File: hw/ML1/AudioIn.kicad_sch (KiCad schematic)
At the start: 23 parts, among them T2 Transformer_1P_1S, U1 LMV324 (Actually LTV9161), U5 LTV-356T

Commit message: Re-work of ML1 board in process
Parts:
- C19, C20: footprint KiCad-Library:CAP_KEMET_530_530 -> bruce-footprints:CAP_KEMET_530_530
- RV2: footprint KiCad-Library:POT_3362P -> bruce-footprints:POT_3362P
- T2: footprint KiCad-Library:CheapAudioTransformer -> bruce-footprints:CheapAudioTransformer
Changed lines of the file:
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@@
       (effects (font (size 1.27 1.27)))
     )
-    (property "Footprint" "KiCad-Library:CheapAudioTransformer" (at 49.53 63.5 0)
+    (property "Footprint" "bruce-footprints:CheapAudioTransformer" (at 49.53 63.5 0)
       (effects (font (size 1.27 1.27)) hide)
     )
@@
       (effects (font (size 1.27 1.27)) (justify right))
     )
-    (property "Footprint" "KiCad-Library:POT_3362P" (at 74.93 62.23 0)
+    (property "Footprint" "bruce-footprints:POT_3362P" (at 74.93 62.23 0)
       (effects (font (size 1.27 1.27)) hide)
     )
@@
       (effects (font (size 1.27 1.27)) (justify left))
     )
-    (property "Footprint" "KiCad-Library:CAP_KEMET_530_530" (at 110.49 88.9 0)
+    (property "Footprint" "bruce-footprints:CAP_KEMET_530_530" (at 110.49 88.9 0)
       (effects (font (size 1.27 1.27)) hide)
     )
@@
       (effects (font (size 1.27 1.27)) (justify left))
     )
-    (property "Footprint" "KiCad-Library:CAP_KEMET_530_530" (at 227.33 34.29 0)
-      (effects (font (size 1.27 1.27)) hide)
-    )
+    (property "Footprint" "bruce-footprints:CAP_KEMET_530_530" (at 227.33 34.29 0)
+      (effects (font (size 1.27 1.27)) hide)
+    )

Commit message: Re-work of ML1 board in process
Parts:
- removed C19: 47u, bruce-footprints:CAP_KEMET_530_530, symbol Device:C_Polarized_US
- removed C20: 100u, bruce-footprints:CAP_KEMET_530_530, symbol Device:C_Polarized_US
- added C19, C20: 47u, Capacitor_SMD:C_0805_2012Metric_Pad1.18x1.45mm_HandSolder, symbol Device:C
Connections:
- net +3.3VA: now also C20.1
- net GNDA: now also C19.2, C20.2
- net at R12.1: now also C19.1
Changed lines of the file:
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@@
+    )
+  )
+  (symbol (lib_id "Device:C") (at 227.33 34.29 0) (unit 1)
+    (in_bom yes) (on_board yes) (dnp no) (fields_autoplaced)
+    (property "Reference" "C20" (at 231.14 33.02 0)
+      (effects (font (size 1.27 1.27)) (justify left))
+    )
+    (property "Value" "47u" (at 231.14 35.56 0)
+      (effects (font (size 1.27 1.27)) (justify left))
+    )
+    (property "Footprint" "Capacitor_SMD:C_0805_2012Metric_Pad1.18x1.45mm_HandSolder" (at 228.2952 38.1 0)
+      (effects (font (size 1.27 1.27)) hide)
+    )
+    (property "Datasheet" "~" (at 227.33 34.29 0)
+      (effects (font (size 1.27 1.27)) hide)
+    )
+    (pin "1")
+    (pin "2")
+    (instances
+      (project "ML1"
+        (path "/5f8f636b-fd0e-498e-8696-0a023acb4c09/605cddf5-737f-47be-b5fd-7ed3decef4e0"
+          (reference "C20") (unit 1)
+        )
+      )
     )
   )
@@
     )
   )
-  (symbol (lib_id "Device:C_Polarized_US") (at 110.49 88.9 0) (unit 1)
-    (in_bom yes) (on_board yes) (dnp no) (fields_autoplaced)
-    (property "Reference" "C19" (at 114.3 86.995 0)
-      (effects (font (size 1.27 1.27)) (justify left))
-    )
-    (property "Value" "47u" (at 114.3 89.535 0)
-      (effects (font (size 1.27 1.27)) (justify left))
-    )
-    (property "Footprint" "bruce-footprints:CAP_KEMET_530_530" (at 110.49 88.9 0)
+  (symbol (lib_id "Device:R_US") (at 127 48.26 90) (unit 1)
+    (in_bom yes) (on_board yes) (dnp no) (fields_autoplaced)
+    (property "Reference" "R13" (at 127 41.91 90)
+      (effects (font (size 1.27 1.27)))
+    )
+    (property "Value" "2.2k" (at 127 44.45 90)
+      (effects (font (size 1.27 1.27)))
+    )
+    (property "Footprint" "Resistor_SMD:R_0805_2012Metric_Pad1.20x1.40mm_HandSolder" (at 127.254 47.244 90)
+      (effects (font (size 1.27 1.27)) hide)
+    )
+    (property "Datasheet" "~" (at 127 48.26 0)
+      (effects (font (size 1.27 1.27)) hide)
+    )
+    (pin "2")
+    (pin "1")
+    (instances
+      (project "ML1"
+        (path "/5f8f636b-fd0e-498e-8696-0a023acb4c09/605cddf5-737f-47be-b5fd-7ed3decef4e0"
+          (reference "R13") (unit 1)
+        )
+      )
+    )
+  )
+  (symbol (lib_id "Device:C") (at 110.49 88.9 0) (unit 1)
+    (in_bom yes) (on_board yes) (dnp no) (fields_autoplaced)
+    (property "Reference" "C19" (at 114.3 87.63 0)
+      (effects (font (size 1.27 1.27)) (justify left))
+    )
+    (property "Value" "47u" (at 114.3 90.17 0)
+      (effects (font (size 1.27 1.27)) (justify left))
+    )
+    (property "Footprint" "Capacitor_SMD:C_0805_2012Metric_Pad1.18x1.45mm_HandSolder" (at 111.4552 92.71 0)
       (effects (font (size 1.27 1.27)) hide)
     )
@@
         (path "/5f8f636b-fd0e-498e-8696-0a023acb4c09/605cddf5-737f-47be-b5fd-7ed3decef4e0"
           (reference "C19") (unit 1)
-        )
-      )
-    )
-  )
-  (symbol (lib_id "Device:R_US") (at 127 48.26 90) (unit 1)
-    (in_bom yes) (on_board yes) (dnp no) (fields_autoplaced)
-    (property "Reference" "R13" (at 127 41.91 90)
-      (effects (font (size 1.27 1.27)))
-    )
-    (property "Value" "2.2k" (at 127 44.45 90)
-      (effects (font (size 1.27 1.27)))
-    )
-    (property "Footprint" "Resistor_SMD:R_0805_2012Metric_Pad1.20x1.40mm_HandSolder" (at 127.254 47.244 90)
-      (effects (font (size 1.27 1.27)) hide)
-    )
-    (property "Datasheet" "~" (at 127 48.26 0)
-      (effects (font (size 1.27 1.27)) hide)
-    )
-    (pin "2")
-    (pin "1")
-    (instances
-      (project "ML1"
-        (path "/5f8f636b-fd0e-498e-8696-0a023acb4c09/605cddf5-737f-47be-b5fd-7ed3decef4e0"
-          (reference "R13") (unit 1)
         )
       )
@@
         )
       )
-    )
-  )
-  (symbol (lib_id "Device:C_Polarized_US") (at 227.33 34.29 0) (unit 1)
-    (in_bom yes) (on_board yes) (dnp no) (fields_autoplaced)
-    (property "Reference" "C20" (at 231.14 32.385 0)
-      (effects (font (size 1.27 1.27)) (justify left))
-    )
-    (property "Value" "100u" (at 231.14 34.925 0)
-      (effects (font (size 1.27 1.27)) (justify left))
-    )
-    (property "Footprint" "bruce-footprints:CAP_KEMET_530_530" (at 227.33 34.29 0)
-      (effects (font (size 1.27 1.27)) hide)
-    )
-    (property "Datasheet" "~" (at 227.33 34.29 0)
-      (effects (font (size 1.27 1.27)) hide)
-    )
-    (pin "2")
-    (pin "1")
-    (instances
-      (project "ML1"
-        (path "/5f8f636b-fd0e-498e-8696-0a023acb4c09/605cddf5-737f-47be-b5fd-7ed3decef4e0"
-          (reference "C20") (unit 1)
-        )
-      )

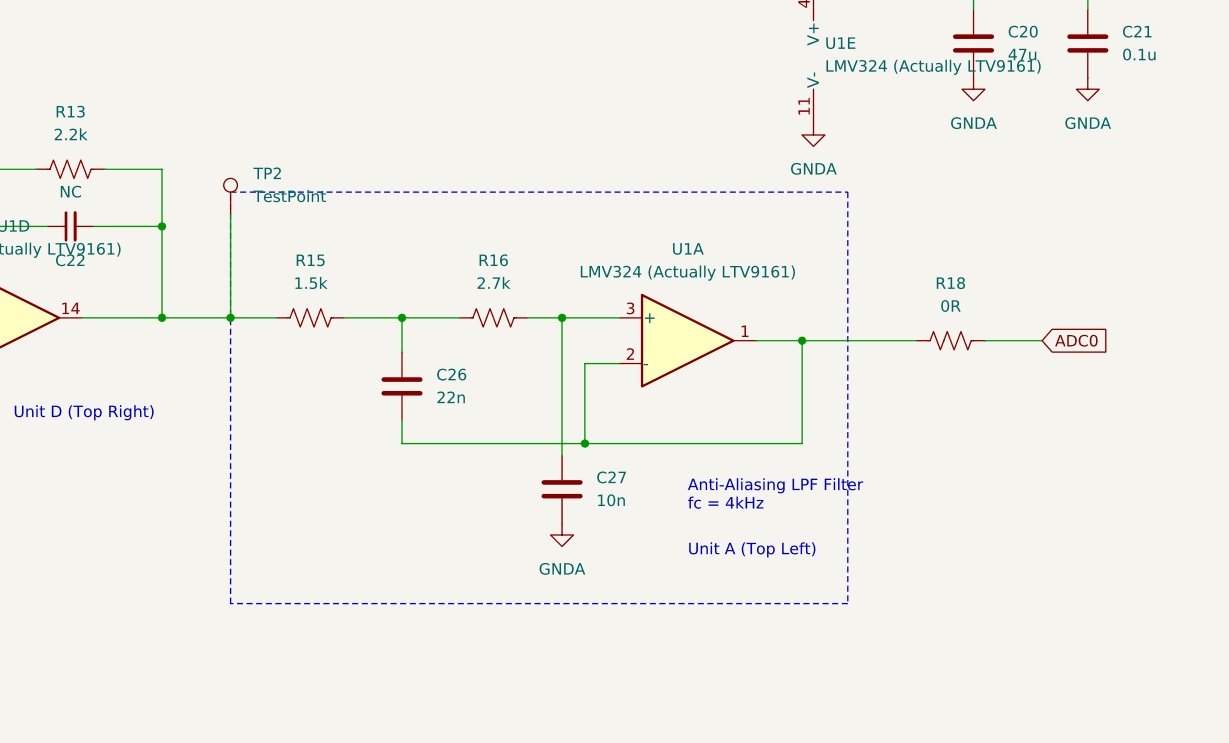
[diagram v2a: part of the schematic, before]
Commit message: First draft of board is passing DRC
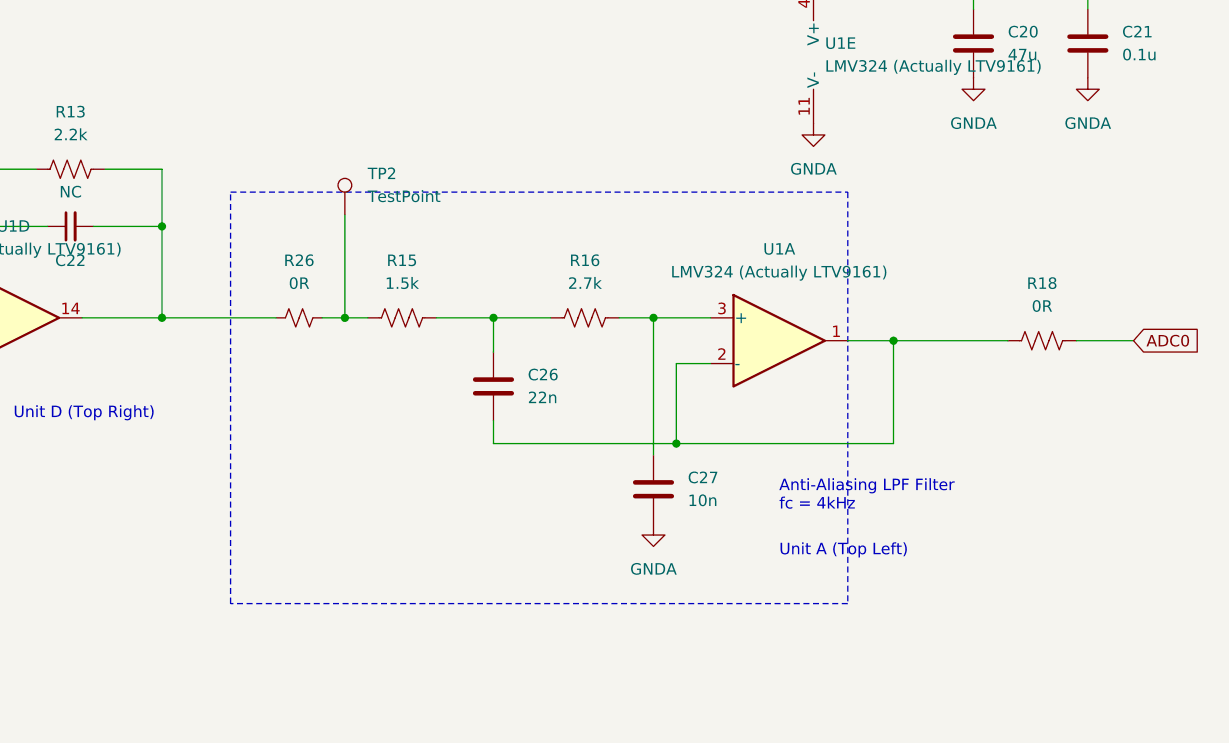
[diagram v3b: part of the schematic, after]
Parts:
- added R26: 0R, Resistor_SMD:R_1206_3216Metric_Pad1.30x1.75mm_HandSolder, symbol Device:R_Small_US
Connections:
- net at C22.2, R13.2, U1.14: now also R26.1; no longer R15.2, TP2.1
- new net: R15.2, R26.2, TP2.1
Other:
- moved on the sheet: C26, C27, R15, R16, R18, TP2, U1A
